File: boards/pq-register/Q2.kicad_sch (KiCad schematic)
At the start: 94 parts, among them Q100 T1-N652, Q65 T1-N652, Q73 T1-N652, Q74 T1-N652, Q75 T1-N652, Q76 T1-N652, Q77 T1-N652, Q78 T1-N652, Q79 T1-N652, Q80 T1-N652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

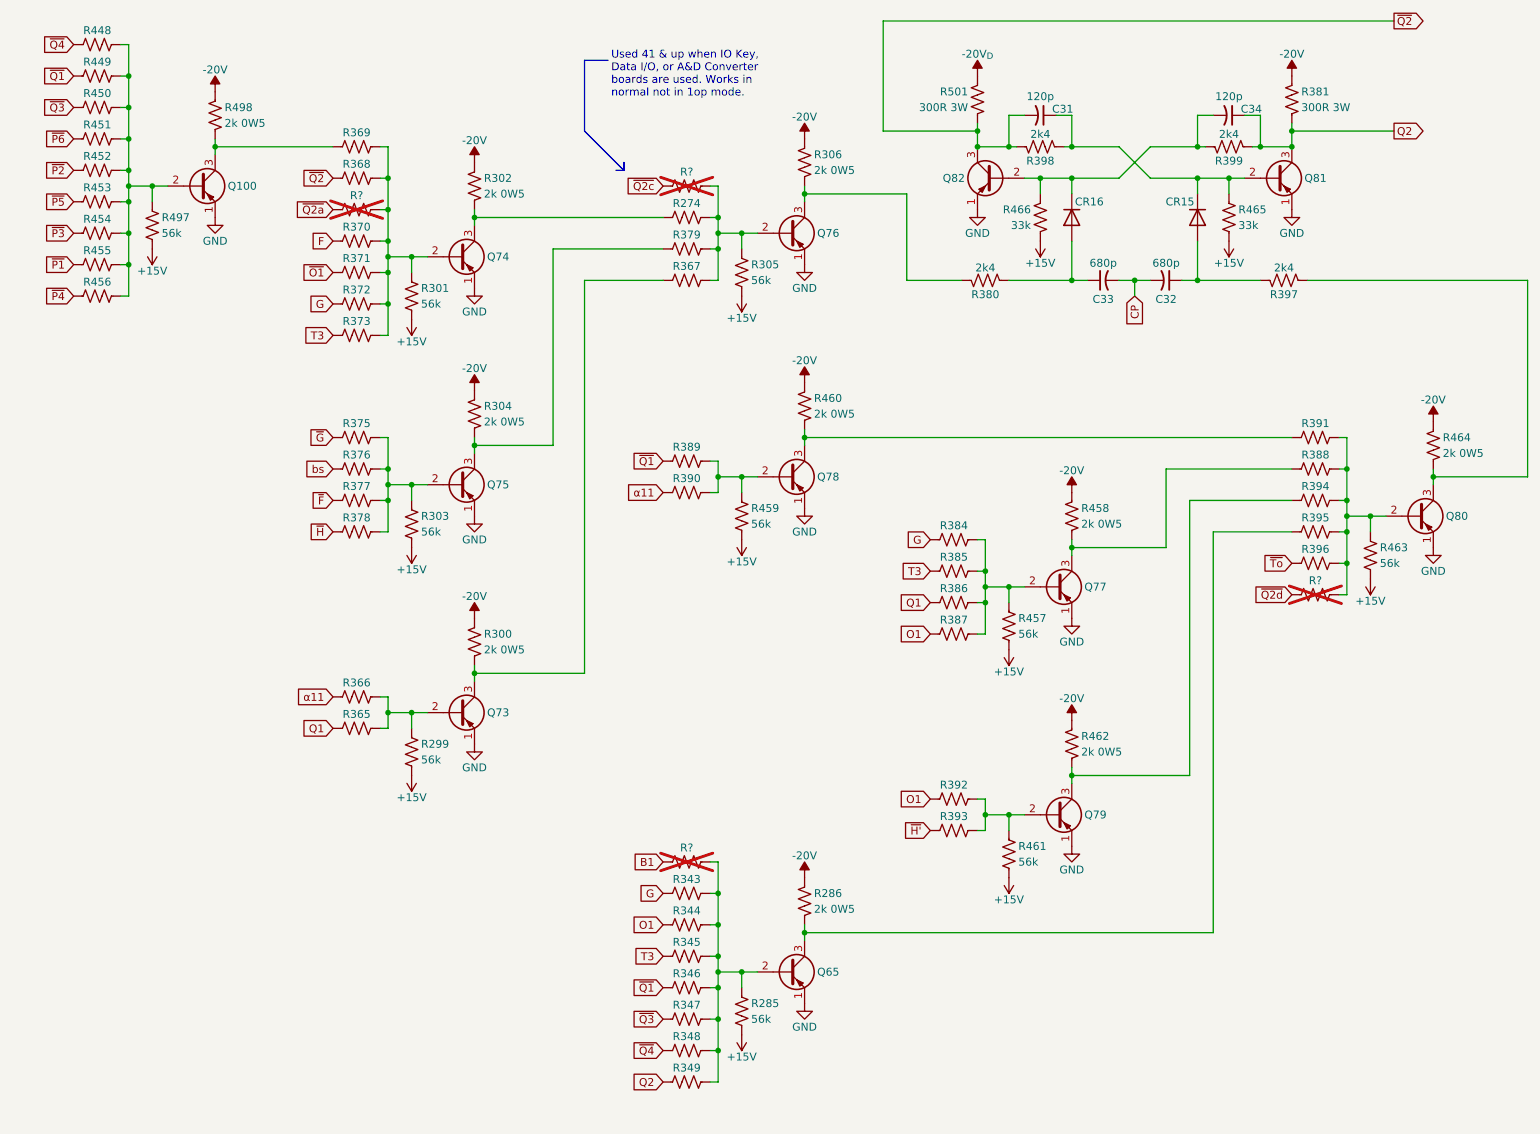
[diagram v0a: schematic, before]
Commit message: Run ERC and clean up P & Q Register board.
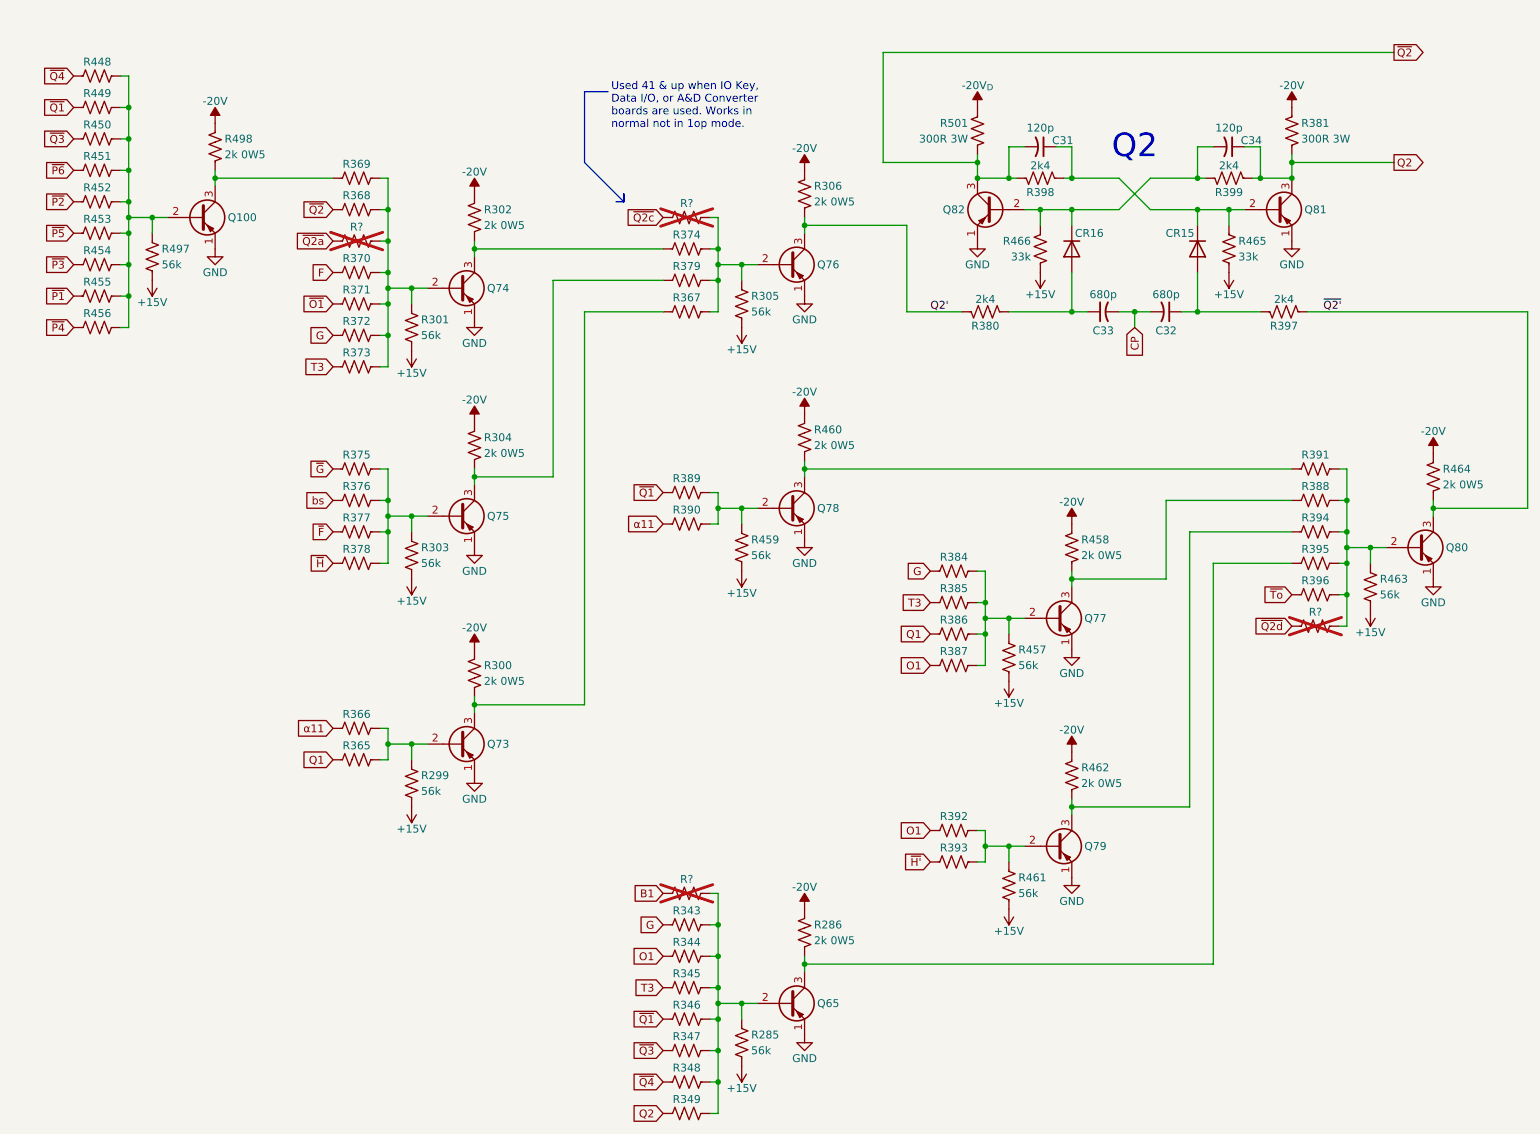
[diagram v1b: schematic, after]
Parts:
- renumbered R274 to R374
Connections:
- net ~{Q2'}: now reaches Q80.3 (C), R397.2, R464.2
- net Q2': now reaches Q76.3 (C), R306.2, R380.1
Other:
- note added: "Q2"
- moved on the sheet: C31, C32, C33, C34, CR15, CR16, Q100, Q65, Q73, Q74, Q75, Q76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

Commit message: Add copyright information.
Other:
- company: (none) -> © 1962 General Precision; redrawn by Sam Hanes
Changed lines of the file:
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@@
 	(title_block
 		(title "LGP-21 P & Q Register Board")
+		(date "2026-06-15")
+		(rev "ESD 1060")
+		(company "© 1962 General Precision; redrawn by Sam Hanes")
+		(comment 1 "https://github.com/Elemecca/lgp21-docs")
 	)
 	(text "Used 41 & up when IO Key,\nData I/O, or A&D Converter\nboards are used. Works in\nnormal not in 1op mode."
